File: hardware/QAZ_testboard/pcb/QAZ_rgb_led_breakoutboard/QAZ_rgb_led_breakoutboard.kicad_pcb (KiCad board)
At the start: 2 copper layers, 25.4 x 25.4 mm, 25 parts, among them J1 Conn_01x01_Male, J2 Conn_01x01_Male, J3 Conn_01x01_Male, J4 Conn_01x01_Male, J5 Conn_01x01_Male, J6 Conn_01x03_Male, J7 Conn_01x03_Male, J8 Conn_01x03_Male, U1 LP5009RUKR

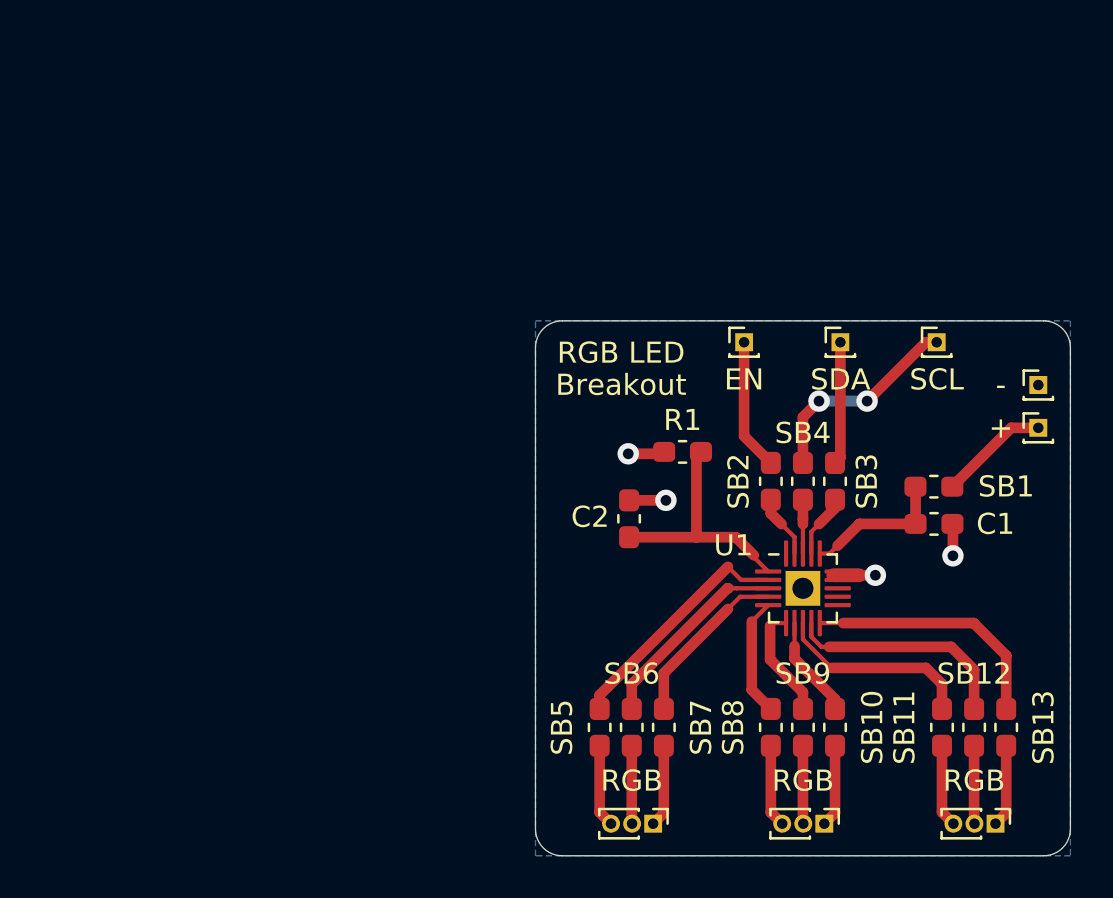
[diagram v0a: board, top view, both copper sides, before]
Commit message: breakout: rgb conversion board
Made a conversion board for the LED driver conversion board. The RGB
LEDs chosen will not fit, and must be replaced in QAZ v1.1.
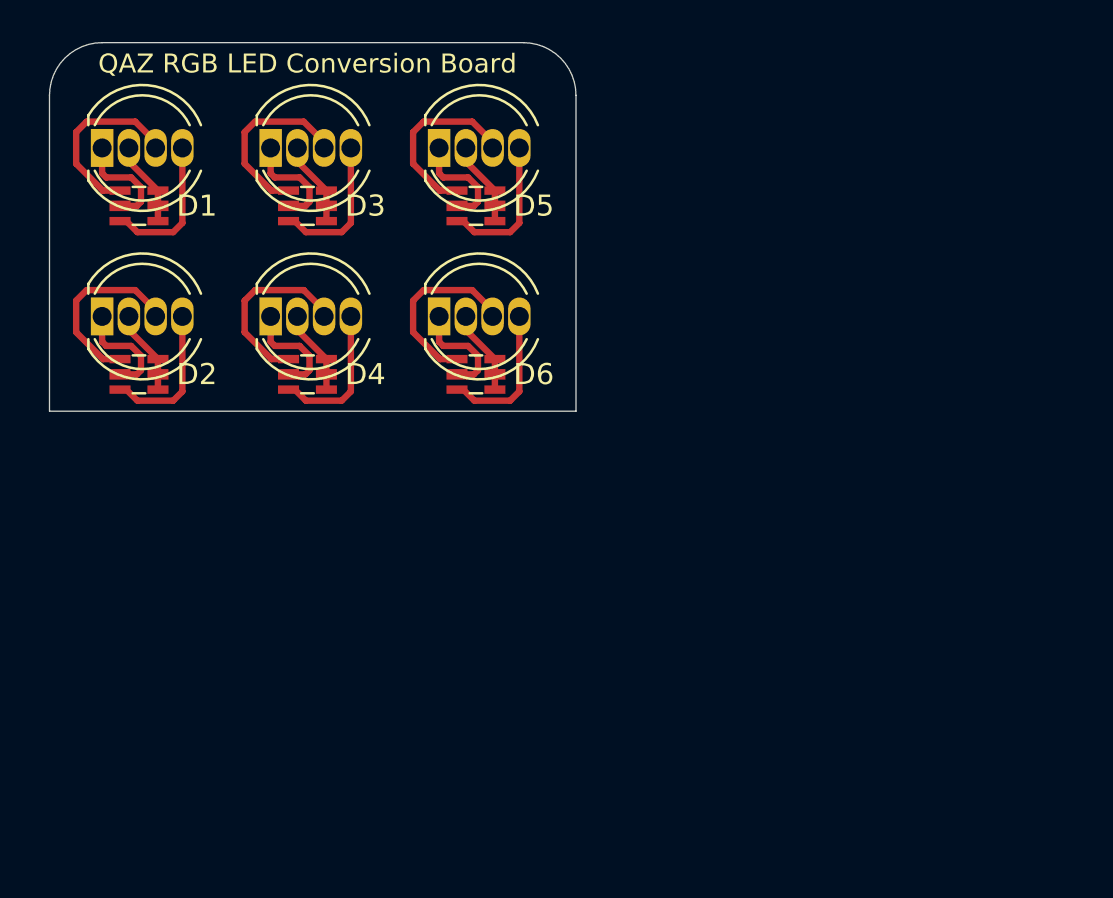
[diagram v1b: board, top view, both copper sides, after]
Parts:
- removed C1, C2: 1uF, Capacitor_SMD:C_0603_1608Metric_Pad1.05x0.95mm_HandSolder
- removed J1, J2, J3, J4, J5: Conn_01x01_Male, Connector_PinHeader_1.00mm:PinHeader_1x01_P1.00mm_Vertical
- removed J6, J7, J8: Conn_01x03_Male, Connector_PinHeader_1.00mm:PinHeader_1x03_P1.00mm_Vertical
- removed R1: 2.1k, Resistor_SMD:R_0603_1608Metric_Pad1.05x0.95mm_HandSolder
- removed SB1, SB10, SB11, SB12, SB13, SB2, SB3, SB4, SB5, SB6, SB7, SB8, SB9: SolderBridge, Resistor_SMD:R_0603_1608Metric_Pad1.05x0.95mm_HandSolder
- removed U1: LP5009RUKR, QAZ:QFN-20-1EP_3x3mm_P0.4mm_EP1.65x1.65mm_HS
- added D1: 19-337C_RSBHGHC-A88_4T, QAZ:0606_1616Metric_HS, F.Cu at (105.6, 65.7)
- added D10: LED_RABG, LED_THT:LED_D5.0mm-4_RGB, F.Cu at (111.9, 70.9)
- added D11: LED_RABG, LED_THT:LED_D5.0mm-4_RGB, F.Cu at (119.9, 62.9)
- added D12: LED_RABG, LED_THT:LED_D5.0mm-4_RGB, F.Cu at (119.9, 70.9)
- added D2: 19-337C_RSBHGHC-A88_4T, QAZ:0606_1616Metric_HS, F.Cu at (105.6, 73.7)
- added D3: 19-337C_RSBHGHC-A88_4T, QAZ:0606_1616Metric_HS, F.Cu at (113.6, 65.7)
- added D4: 19-337C_RSBHGHC-A88_4T, QAZ:0606_1616Metric_HS, F.Cu at (113.6, 73.7)
- added D5: 19-337C_RSBHGHC-A88_4T, QAZ:0606_1616Metric_HS, F.Cu at (121.6, 65.7)
- added D6: 19-337C_RSBHGHC-A88_4T, QAZ:0606_1616Metric_HS, F.Cu at (121.6, 73.7)
- added D7: LED_RABG, LED_THT:LED_D5.0mm-4_RGB, F.Cu at (103.9, 62.9)
- added D8: LED_RABG, LED_THT:LED_D5.0mm-4_RGB, F.Cu at (103.9, 70.9)
- added D9: LED_RABG, LED_THT:LED_D5.0mm-4_RGB, F.Cu at (111.9, 62.9)
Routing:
- net Net-(SB13-Pad1): track 12.0 -> 0.00 mm
- net Net-(C2-Pad1): track 11.6 -> 0.00 mm
- net Net-(SB5-Pad1): track 11.4 -> 0.00 mm
- net Net-(SB12-Pad1): track 10.9 -> 0.00 mm
- net /LED_SCL: track 10.00 -> 0.00 mm, vias 2 -> 0
- net Net-(SB6-Pad1): track 9.54 -> 0.00 mm
- net Net-(SB11-Pad1): track 9.44 -> 0.00 mm
- net Net-(D3-Pad5): track 0.00 -> 8.78 mm
- net Net-(D2-Pad5): track 0.00 -> 8.78 mm
- net Net-(D12-Pad3): track 0.00 -> 8.78 mm
- net Net-(D11-Pad3): track 0.00 -> 8.78 mm
- net Net-(D10-Pad3): track 0.00 -> 8.78 mm
- net Net-(D1-Pad5): track 0.00 -> 8.78 mm
- net Net-(SB7-Pad1): track 8.16 -> 0.00 mm
- net GND: track 7.02 -> 0.00 mm, vias 4 -> 0
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- removed copper zone on B.Cu, net GND
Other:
- board size 25.4 x 25.4 mm -> 25 x 17.5 mm
- board text added: "QAZ RGB LED Conversion Board"
- board text removed: "+"
- board text removed: "-"
- board text removed: "Breakout"
- board text removed: "EN"
- board text removed: "RGB"
- board text removed: "RGB LED"
- board text removed: "SCL"
- board text removed: "SDA"
